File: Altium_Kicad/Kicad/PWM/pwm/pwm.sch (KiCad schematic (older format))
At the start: 12 parts, among them U1 Opamp_Dual_Generic, U2 LM319

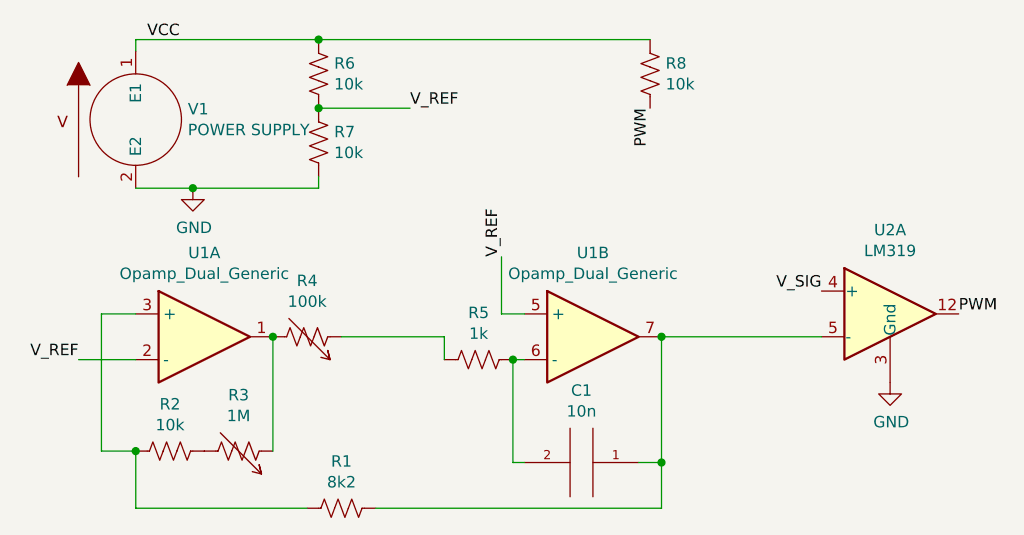
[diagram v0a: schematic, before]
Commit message: Draft lab, fixed PWm gen schematic by adding rail definition
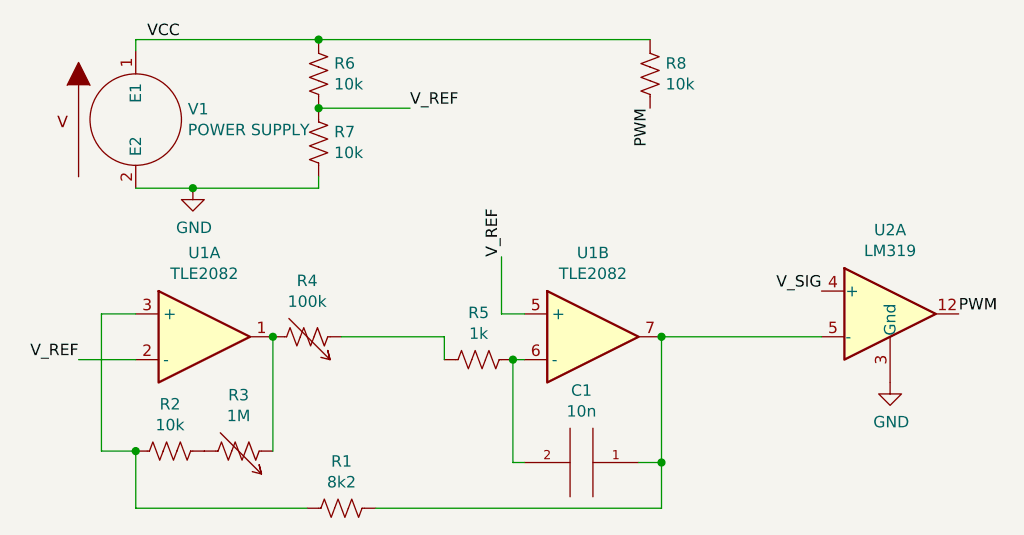
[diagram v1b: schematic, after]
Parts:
- U1: value Opamp_Dual_Generic -> TLE2082
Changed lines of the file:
@@
 P 2350 1900
 F 0 "U1" H 2350 2267 50  0000 C CNN
-F 1 "Opamp_Dual_Generic" H 2350 2176 50  0000 C CNN
+F 1 "TLE2082" H 2350 2176 50  0000 C CNN
 F 2 "" H 2350 1900 50  0001 C CNN
 F 3 "~" H 2350 1900 50  0001 C CNN
@@
 P 4050 1900
 F 0 "U1" H 4050 2267 50  0000 C CNN
-F 1 "Opamp_Dual_Generic" H 4050 2176 50  0000 C CNN
+F 1 "TLE2082" H 4050 2176 50  0000 C CNN
 F 2 "" H 4050 1900 50  0001 C CNN
 F 3 "~" H 4050 1900 50  0001 C CNN

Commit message: Resync
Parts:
- added unit 3 of U1
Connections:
- net GND: now also U1.4 (V-)
- net VCC: now also U1.8 (V+)
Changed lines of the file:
@@
 Text Label 4300 900  3    50   ~ 0
 PWM
+$Comp
+L Device:Opamp_Dual_Generic U1
+U 3 1 5E6D8DAD
+P 5000 900
+F 0 "U1" H 4958 946 50  0000 L CNN
+F 1 "TLE2082" H 4958 855 50  0000 L CNN
+F 2 "" H 5000 900 50  0001 C CNN
+F 3 "~" H 5000 900 50  0001 C CNN
+	3    5000 900
+	1    0    0    -1
+$EndComp
+Wire Wire Line
+	4300 600  4900 600
+Connection ~ 4300 600
+$Comp
+L power:GND #PWR?
+U 1 1 5E6DAD62
+P 4900 1200
+F 0 "#PWR?" H 4900 950 50  0001 C CNN
+F 1 "GND" H 4905 1027 50  0000 C CNN
+F 2 "" H 4900 1200 50  0001 C CNN
+F 3 "" H 4900 1200 50  0001 C CNN
+	1    4900 1200
+	1    0    0    -1
+$EndComp
 $EndSCHEMATC
